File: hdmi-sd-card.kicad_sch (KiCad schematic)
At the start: 92 parts, among them J11 I-PEX_CABLINE-VS_1x20_20455-A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, J4 HDMI-A_WE_685119134923, J5 MicroSD_693071020811, Q18 BSS138PW, Q19 BSS138PW, Q21 BSS138PW, U10 TPD4E05U06QDQARQ1, U11 TPD4E05U06QDQARQ1, U12 TPD4E05U06QDQARQ1, U14 TPD4E05U06QDQARQ1, U37 TPD4E05U06QDQARQ1, U38 SN65DP159RGZR, U40 NVT4858_XQFN, U41 TPD4E05U06QDQARQ1, U42 M24C64-F_DFN8, U43 TPS2116DRLR, U44 TXS0102DQER, U47 TPD4E05U06QDQARQ1, U48 TPD4E05U06QDQARQ1

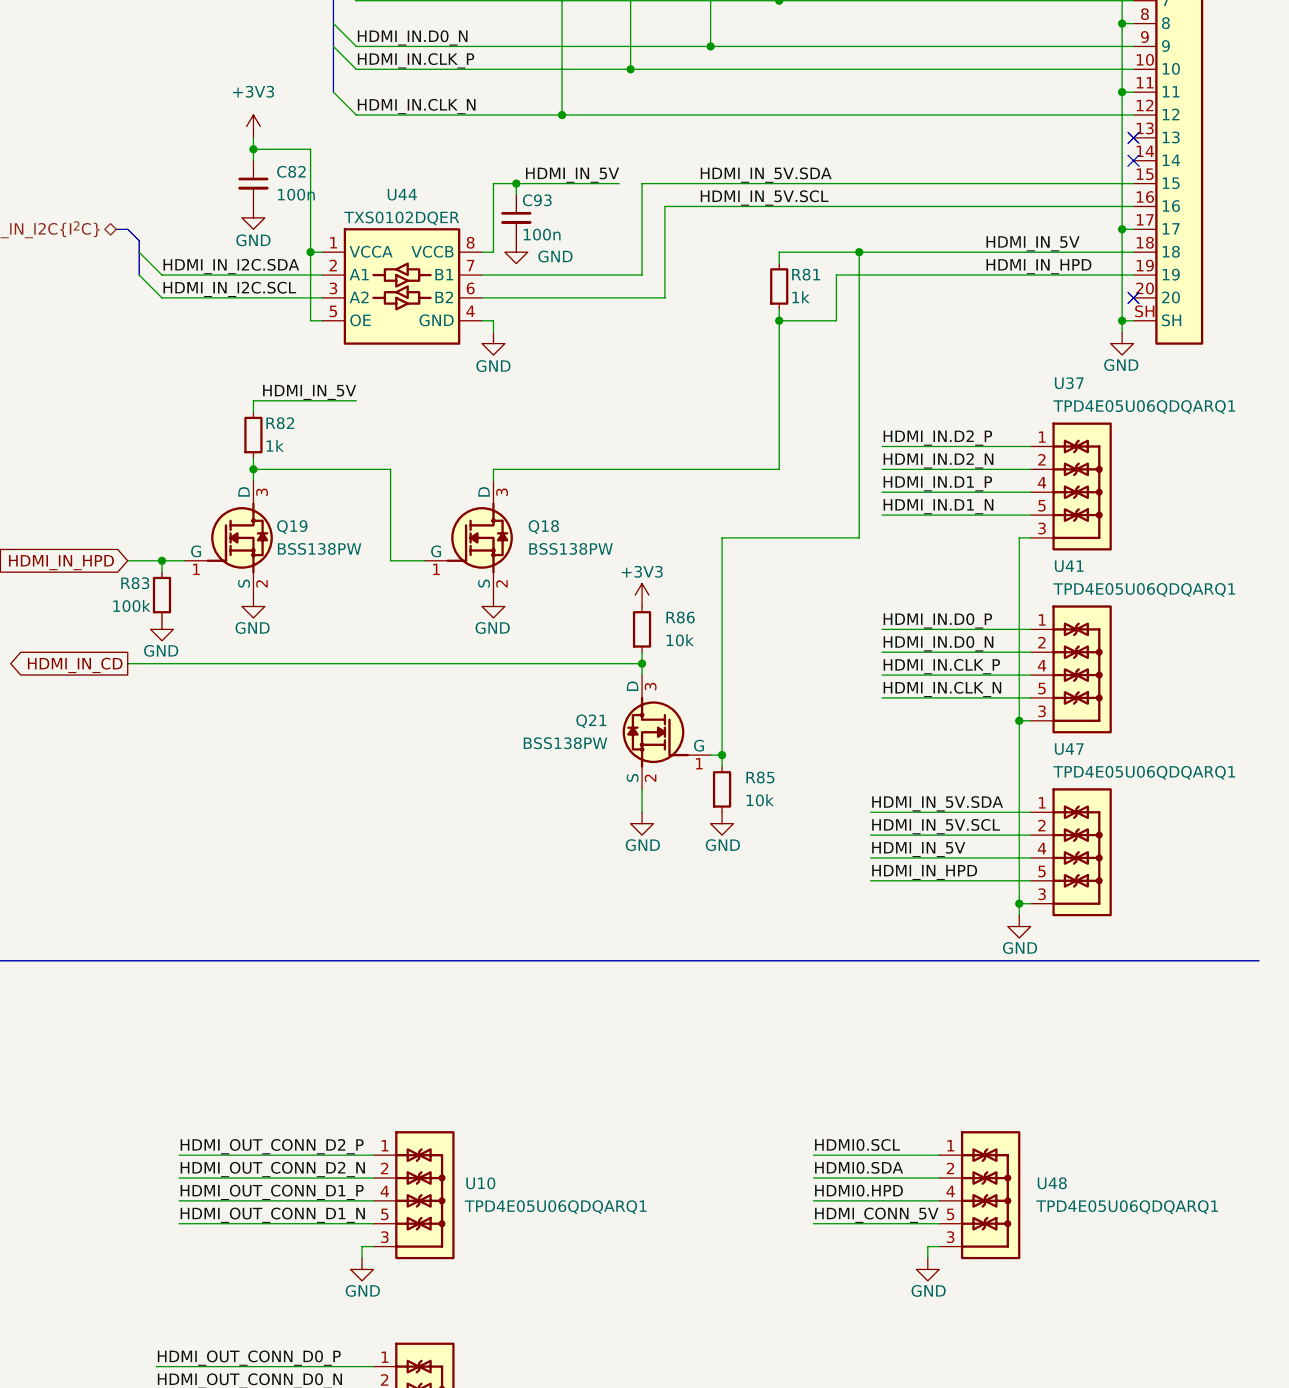
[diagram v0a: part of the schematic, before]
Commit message: [#67276] HDMI Routing
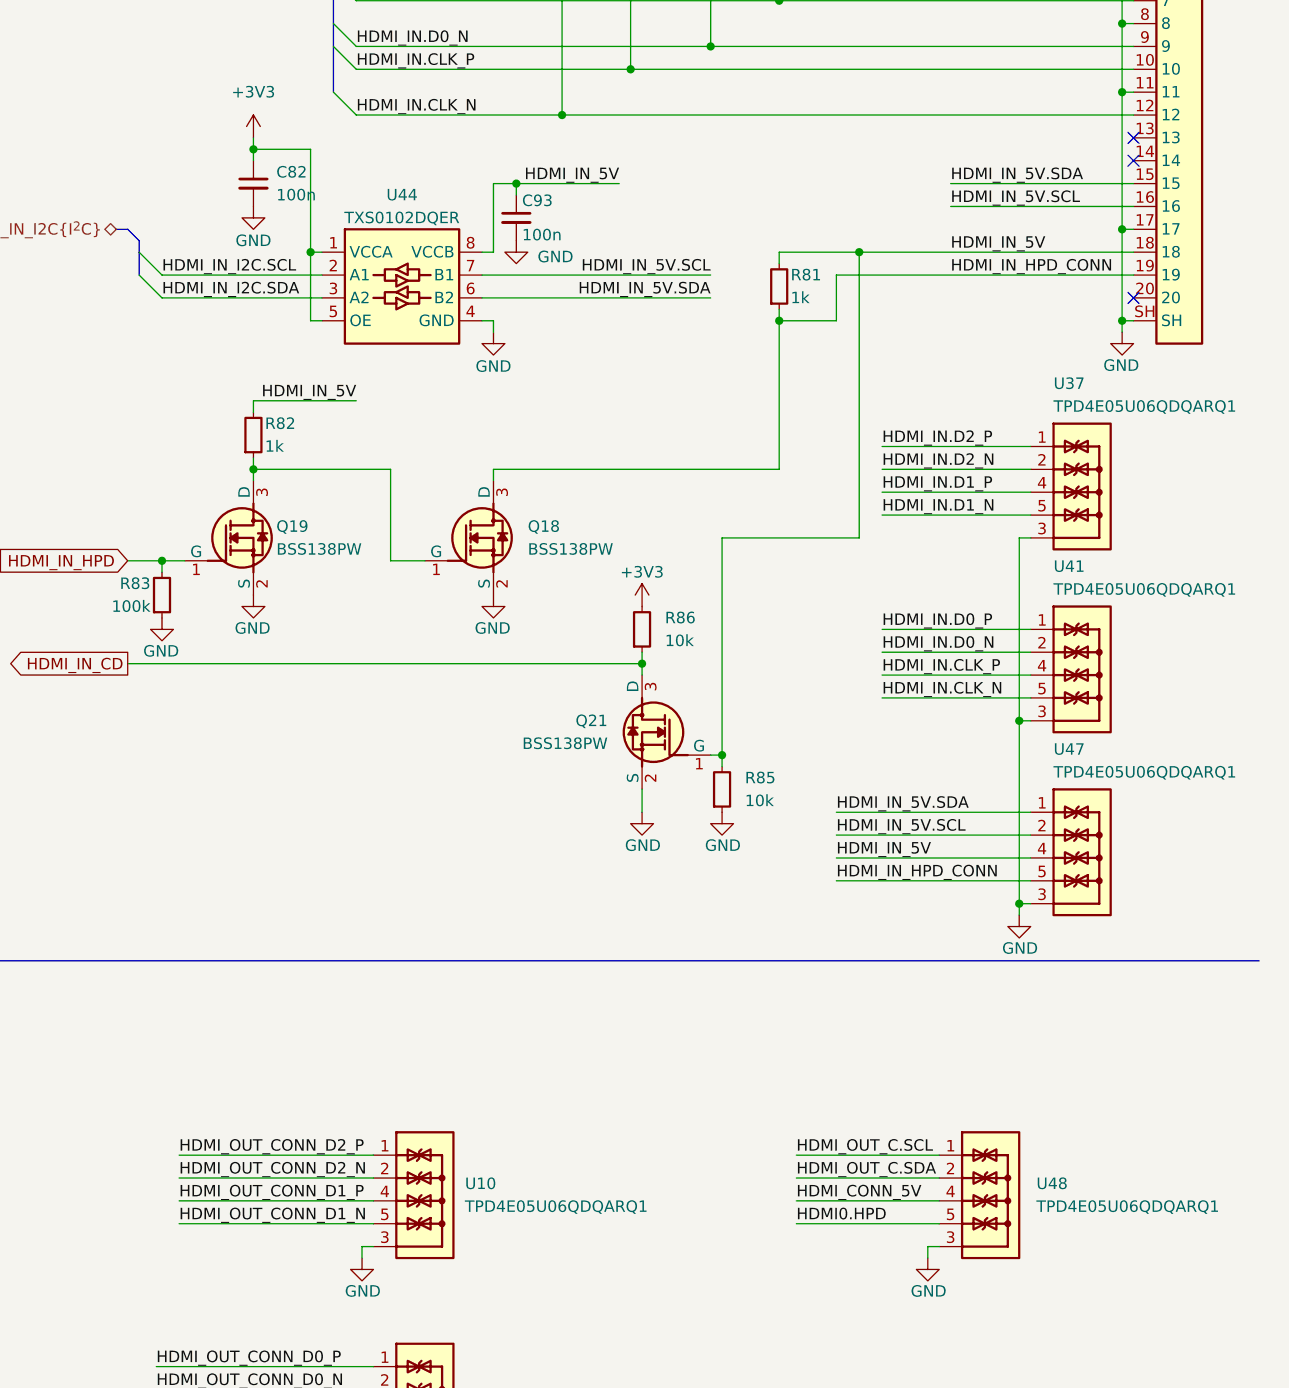
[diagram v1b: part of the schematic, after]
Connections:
- net HDMI0.SCL is gone; now on net HDMI_OUT_C.SCL: U48.1, U48.10
- net HDMI0.SDA is gone; now on net HDMI_OUT_C.SDA: U48.2, U48.9
- net HDMI0.HPD: now also U48.5, U48.6; no longer U48.4, U48.7
- net HDMI_CONN_5V: now also U48.4, U48.7; no longer U48.5, U48.6
- net HDMI_IN_5V.SCL: now also U44.7 (B1); no longer U44.6 (B2)
- net HDMI_IN_5V.SDA: now also U44.6 (B2); no longer U44.7 (B1)
- net HDMI_IN_HPD: no longer J11.19, Q18.3 (D), R81.1, U47.5, U47.6
- net HDMI_IN_I2C.SCL: now also U44.2 (A1); no longer U44.3 (A2)
- net HDMI_IN_I2C.SDA: now also U44.3 (A2); no longer U44.2 (A1)
- new net HDMI_IN_HPD_CONN: J11.19, Q18.3 (D), R81.1, U47.5, U47.6
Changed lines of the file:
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@@
     (stroke (width 0) (type default))
   )
-  (wire (pts (xy 356.87 190.5) (xy 370.84 190.5))
+  (wire (pts (xy 354.965 190.5) (xy 370.84 190.5))
     (stroke (width 0) (type default))
   )
@@
     (stroke (width 0) (type default))
   )
-  (wire (pts (xy 356.87 198.12) (xy 370.84 198.12))
+  (wire (pts (xy 354.965 198.12) (xy 370.84 198.12))
     (stroke (width 0) (type default))
   )
@@
     (stroke (width 0) (type default))
   )
-  (wire (pts (xy 337.82 92.71) (xy 337.82 82.55))
-    (stroke (width 0) (type default))
-  )
   (wire (pts (xy 337.82 152.4) (xy 337.82 149.86))
     (stroke (width 0) (type default))
@@
     (stroke (width 0) (type default))
   )
+  (wire (pts (xy 359.41 152.4) (xy 381 152.4))
+    (stroke (width 0) (type default))
+  )
   (bus (pts (xy 55.245 158.75) (xy 55.245 160.02))
     (stroke (width 0) (type default))
@@
     (stroke (width 0) (type default))
   )
+  (wire (pts (xy 359.41 154.94) (xy 381 154.94))
+    (stroke (width 0) (type default))
+  )
   (wire (pts (xy 345.44 27.94) (xy 353.06 27.94))
     (stroke (width 0) (type default))
@@
     (stroke (width 0) (type default))
   )
-  (wire (pts (xy 340.36 85.09) (xy 392.43 85.09))
-    (stroke (width 0) (type default))
-  )
   (wire (pts (xy 36.83 268.605) (xy 64.135 268.605))
     (stroke (width 0) (type default))
@@
     (stroke (width 0) (type default))
   )
-  (wire (pts (xy 363.22 152.4) (xy 381 152.4))
-    (stroke (width 0) (type default))
-  )
   (wire (pts (xy 321.31 97.79) (xy 321.31 99.06))
     (stroke (width 0) (type default))
@@
     (stroke (width 0) (type default))
   )
-  (wire (pts (xy 363.22 160.02) (xy 381 160.02))
-    (stroke (width 0) (type default))
-  )
   (wire (pts (xy 294.64 106.68) (xy 306.07 106.68))
     (stroke (width 0) (type default))
@@
     (stroke (width 0) (type default))
   )
-  (wire (pts (xy 320.04 95.25) (xy 340.36 95.25))
+  (wire (pts (xy 320.04 95.25) (xy 345.44 95.25))
     (stroke (width 0) (type default))
   )
@@
     (stroke (width 0) (type default))
   )
+  (wire (pts (xy 372.11 85.09) (xy 392.43 85.09))
+    (stroke (width 0) (type default))
+  )
   (wire (pts (xy 31.75 263.525) (xy 25.4 263.525))
     (stroke (width 0) (type default))
@@
     (stroke (width 0) (type default))
   )
-  (wire (pts (xy 363.22 157.48) (xy 381 157.48))
+  (wire (pts (xy 359.41 157.48) (xy 381 157.48))
     (stroke (width 0) (type default))
   )
@@
     (stroke (width 0) (type default))
   )
+  (wire (pts (xy 359.41 160.02) (xy 381 160.02))
+    (stroke (width 0) (type default))
+  )
   (wire (pts (xy 76.2 74.93) (xy 80.01 74.93))
     (stroke (width 0) (type default))
@@
     (stroke (width 0) (type default))
   )
-  (wire (pts (xy 363.22 154.94) (xy 381 154.94))
-    (stroke (width 0) (type default))
-  )
   (wire (pts (xy 67.31 33.655) (xy 67.31 32.385))
     (stroke (width 0) (type default))
@@
     (stroke (width 0) (type default))
   )
-  (wire (pts (xy 356.87 193.04) (xy 370.84 193.04))
+  (wire (pts (xy 354.965 193.04) (xy 370.84 193.04))
     (stroke (width 0) (type default))
   )
@@
     (stroke (width 0) (type default))
   )
+  (wire (pts (xy 372.11 82.55) (xy 392.43 82.55))
+    (stroke (width 0) (type default))
+  )
   (wire (pts (xy 57.785 50.8) (xy 57.785 54.61))
     (stroke (width 0) (type default))
@@
     (stroke (width 0) (type default))
   )
-  (wire (pts (xy 340.36 95.25) (xy 340.36 85.09))
-    (stroke (width 0) (type default))
-  )
   (wire (pts (xy 80.01 57.15) (xy 76.2 57.15))
     (stroke (width 0) (type default))
@@
     (stroke (width 0) (type default))
   )
-  (wire (pts (xy 356.87 195.58) (xy 370.84 195.58))
+  (wire (pts (xy 354.965 195.58) (xy 370.84 195.58))
     (stroke (width 0) (type default))
   )
@@
     (stroke (width 0) (type default))
   )
-  (wire (pts (xy 320.04 92.71) (xy 337.82 92.71))
+  (wire (pts (xy 320.04 92.71) (xy 345.44 92.71))
     (stroke (width 0) (type default))
   )
@@
   )
   (wire (pts (xy 77.47 227.33) (xy 63.5 227.33))
-    (stroke (width 0) (type default))
-  )
-  (wire (pts (xy 337.82 82.55) (xy 392.43 82.55))
     (stroke (width 0) (type default))
   )
@@
     (effects (font (size 2.9972 2.9972) (thickness 0.5994) bold) (justify left bottom))
   )
+  (label "HDMI_IN_5V.SCL" (at 345.44 92.71 180) (fields_autoplaced)
+    (effects (font (size 1.27 1.27)) (justify right bottom))
+  )
   (label "HDMI_OUT_CONN_D1_P" (at 207.01 200.66 0) (fields_autoplaced)
     (effects (font (size 1.27 1.27)) (justify left bottom))
@@
     (effects (font (size 1.27 1.27)) (justify left bottom))
   )
-  (label "HDMI_IN_HPD" (at 363.22 160.02 0) (fields_autoplaced)
+  (label "HDMI_IN_HPD_CONN" (at 359.41 160.02 0) (fields_autoplaced)
     (effects (font (size 1.27 1.27)) (justify left bottom))
   )
@@
     (effects (font (size 1.27 1.27)) (justify left bottom))
   )
+  (label "HDMI_OUT_C.SCL" (at 354.965 190.5 0) (fields_autoplaced)
+    (effects (font (size 1.27 1.27)) (justify left bottom))
+  )
   (label "HDMI_CTL.SDA" (at 114.3 229.87 0) (fields_autoplaced)
     (effects (font (size 1.27 1.27)) (justify left bottom))
@@
     (effects (font (size 1.27 1.27)) (justify left bottom))
   )
-  (label "HDMI_CONN_5V" (at 356.87 198.12 0) (fields_autoplaced)
+  (label "HDMI_CONN_5V" (at 354.965 195.58 0) (fields_autoplaced)
     (effects (font (size 1.27 1.27)) (justify left bottom))
   )
@@
     (effects (font (size 1.27 1.27)) (justify right bottom))
   )
-  (label "HDMI0.HPD" (at 356.87 195.58 0) (fields_autoplaced)
+  (label "HDMI0.HPD" (at 354.965 198.12 0) (fields_autoplaced)
     (effects (font (size 1.27 1.27)) (justify left bottom))
   )
@@
     (effects (font (size 1.27 1.27)) (justify left bottom))
   )
-  (label "HDMI_IN_HPD" (at 375.92 92.71 0) (fields_autoplaced)
+  (label "HDMI_IN_HPD_CONN" (at 372.11 92.71 0) (fields_autoplaced)
     (effects (font (size 1.27 1.27)) (justify left bottom))
   )
@@
     (effects (font (size 1.27 1.27)) (justify left bottom))
   )
-  (label "HDMI_IN_5V.SDA" (at 344.17 82.55 0) (fields_autoplaced)
+  (label "HDMI_IN_5V.SDA" (at 372.11 82.55 0) (fields_autoplaced)
     (effects (font (size 1.27 1.27)) (justify left bottom))
   )
@@
     (effects (font (size 1.27 1.27)) (justify right bottom))
   )
-  (label "HDMI_IN_5V.SCL" (at 363.22 154.94 0) (fields_autoplaced)
+  (label "HDMI_IN_5V.SCL" (at 359.41 154.94 0) (fields_autoplaced)
     (effects (font (size 1.27 1.27)) (justify left bottom))
   )
@@
     (effects (font (size 1.27 1.27)) (justify left bottom))
   )
-  (label "HDMI0.SDA" (at 356.87 193.04 0) (fields_autoplaced)
-    (effects (font (size 1.27 1.27)) (justify left bottom))
-  )
   (label "I2C_EN{slash}PIN" (at 62.23 208.28 0) (fields_autoplaced)
     (effects (font (size 1.27 1.27)) (justify left bottom))
@@
     (effects (font (size 1.27 1.27)) (justify left bottom))
   )
-  (label "HDMI_IN_5V" (at 363.22 157.48 0) (fields_autoplaced)
+  (label "HDMI_IN_5V" (at 359.41 157.48 0) (fields_autoplaced)
     (effects (font (size 1.27 1.27)) (justify left bottom))
   )
@@
     (effects (font (size 1.27 1.27)) (justify left bottom))
   )
+  (label "HDMI_OUT_C.SDA" (at 354.965 193.04 0) (fields_autoplaced)
+    (effects (font (size 1.27 1.27)) (justify left bottom))
+  )
   (label "HDMI_OUT_CONN_D0_P" (at 283.845 213.995 0) (fields_autoplaced)
     (effects (font (size 1.27 1.27)) (justify left bottom))
   )
-  (label "HDMI_IN_5V.SCL" (at 344.17 85.09 0) (fields_autoplaced)
+  (label "HDMI_IN_5V.SCL" (at 372.11 85.09 0) (fields_autoplaced)
     (effects (font (size 1.27 1.27)) (justify left bottom))
   )
@@
     (effects (font (size 1.27 1.27)) (justify right bottom))
   )
-  (label "HDMI0.SCL" (at 356.87 190.5 0) (fields_autoplaced)
-    (effects (font (size 1.27 1.27)) (justify left bottom))
-  )
   (label "SD_CLK" (at 144.78 59.69 0) (fields_autoplaced)
     (effects (font (size 1.27 1.27)) (justify left bottom))
@@
     (effects (font (size 1.27 1.27)) (justify left bottom))
   )
-  (label "HDMI_IN_5V" (at 375.92 90.17 0) (fields_autoplaced)
+  (label "HDMI_IN_5V.SDA" (at 345.44 95.25 180) (fields_autoplaced)
+    (effects (font (size 1.27 1.27)) (justify right bottom))
+  )
+  (label "HDMI_IN_5V" (at 372.11 90.17 0) (fields_autoplaced)
     (effects (font (size 1.27 1.27)) (justify left bottom))
   )
@@
     (effects (font (size 1.27 1.27)) (justify left bottom))
   )
-  (label "HDMI_IN_I2C.SCL" (at 284.48 95.25 0) (fields_autoplaced)
+  (label "HDMI_IN_I2C.SCL" (at 284.48 92.71 0) (fields_autoplaced)
     (effects (font (size 1.27 1.27)) (justify left bottom))
   )
@@
     (effects (font (size 1.27 1.27)) (justify left bottom))
   )
-  (label "HDMI_IN_I2C.SDA" (at 284.48 92.71 0) (fields_autoplaced)
+  (label "HDMI_IN_I2C.SDA" (at 284.48 95.25 0) (fields_autoplaced)
     (effects (font (size 1.27 1.27)) (justify left bottom))
   )
@@
     (effects (font (size 1.27 1.27)) (justify left bottom))
   )
-  (label "HDMI_IN_5V.SDA" (at 363.22 152.4 0) (fields_autoplaced)
-    (effects (font (size 1.27 1.27)) (justify left bottom))
-  )
+  (label "HDMI_IN_5V.SDA" (at 359.41 152.4 0) (fields_autoplaced)
+    (effects (font (size 1.27 1.27)) (justify left bottom))
+  )
